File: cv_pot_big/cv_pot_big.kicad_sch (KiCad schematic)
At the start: 13 parts, among them J1 I/O connector, U1 HT7550-1, U2 TLV6001UIDBVR

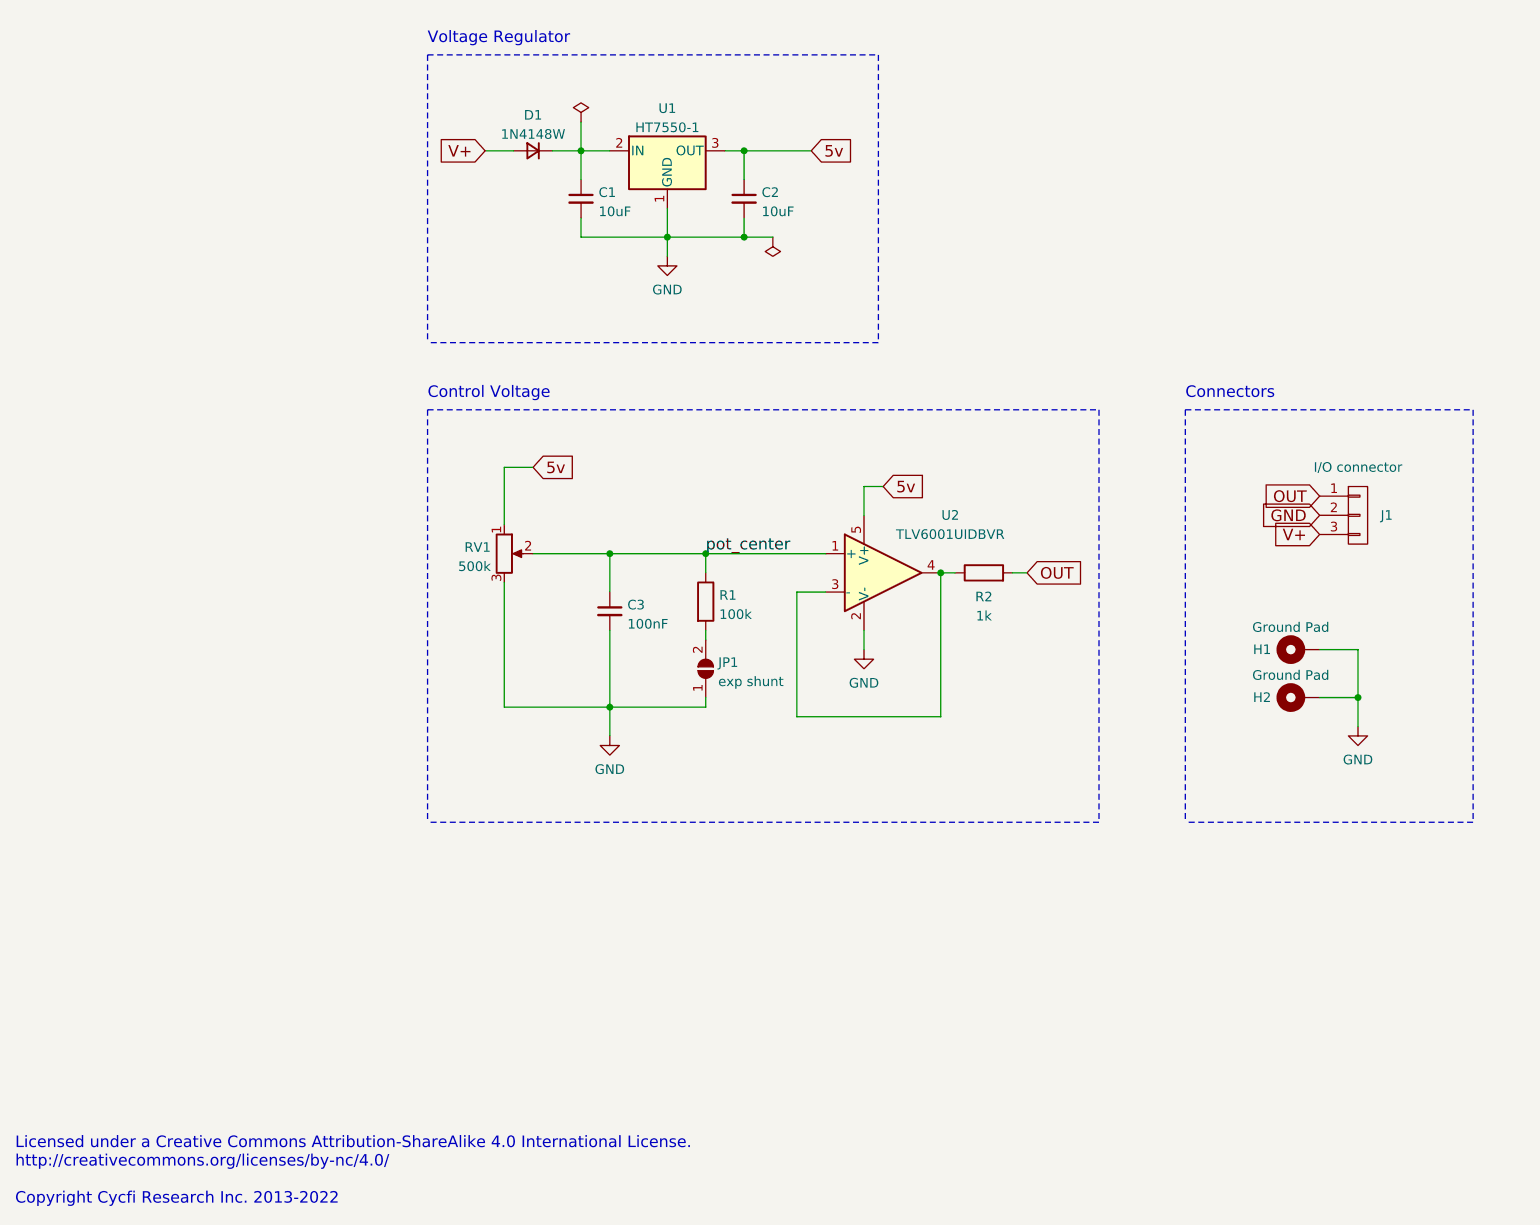
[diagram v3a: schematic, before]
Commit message: Update with log and exp taper
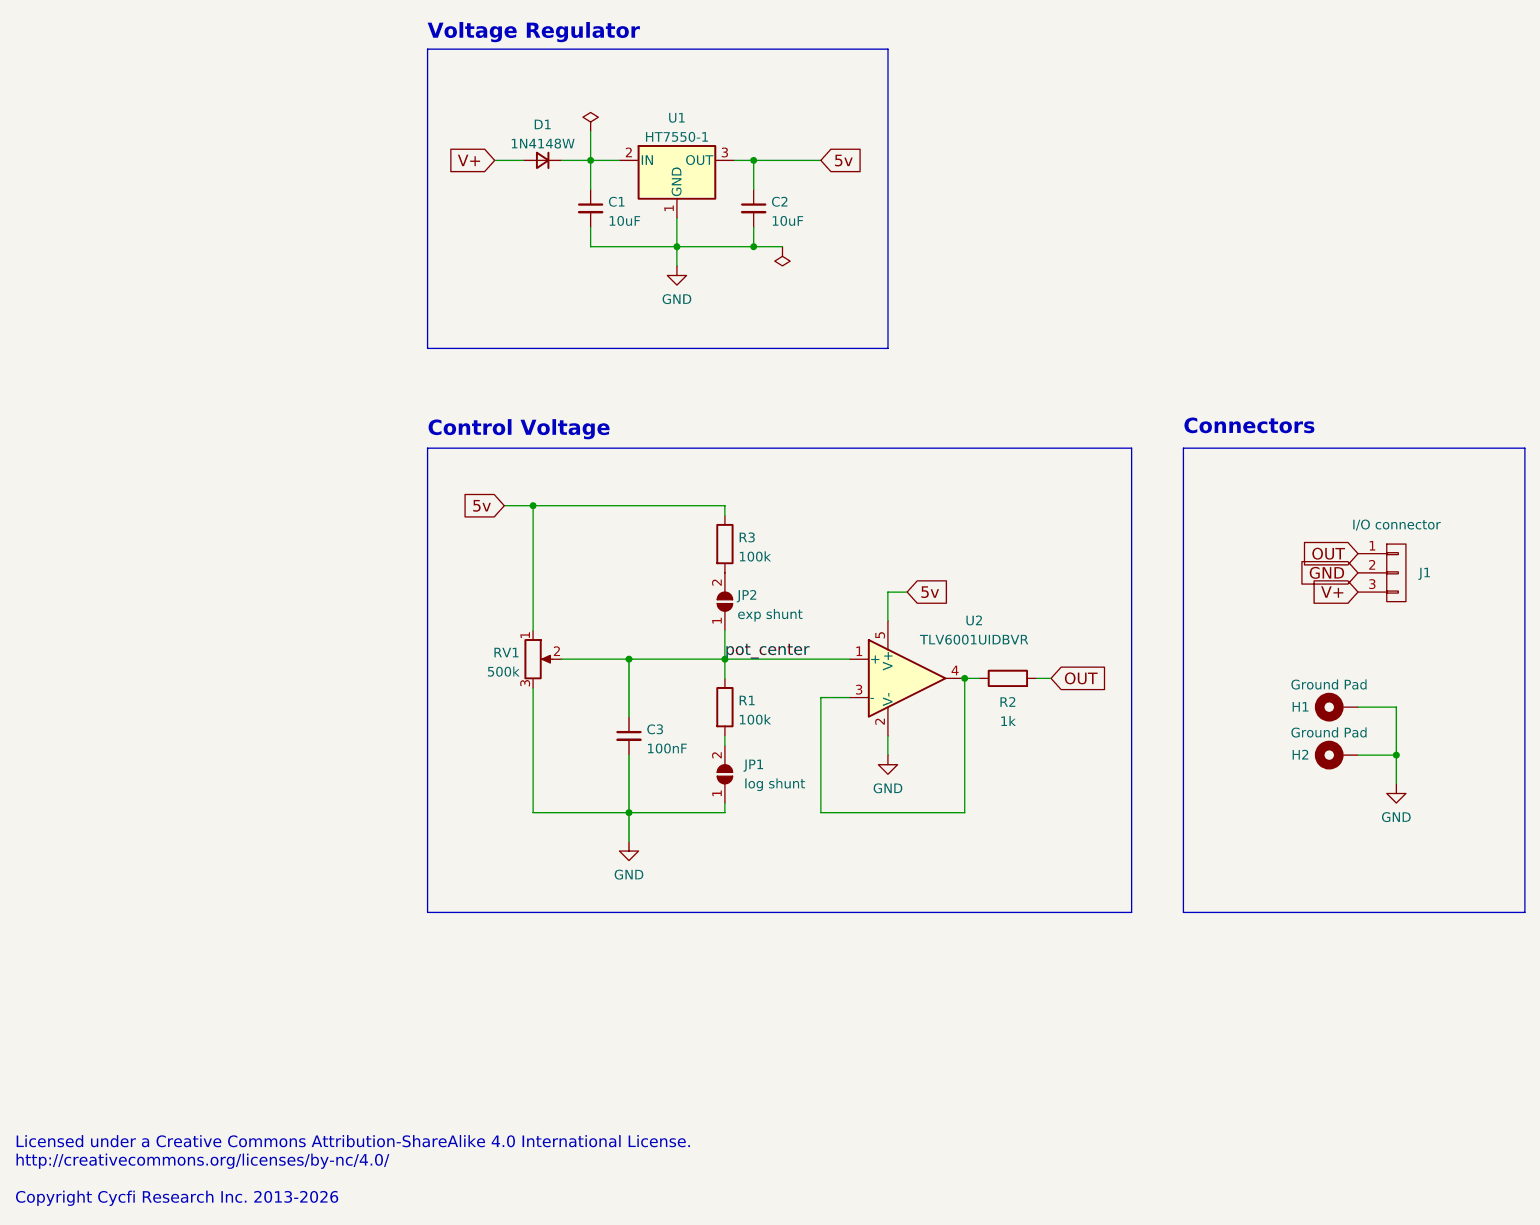
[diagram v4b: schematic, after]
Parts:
- added JP2: exp shunt, Jumper:SolderJumper-2_P1.3mm_Open_TrianglePad1.0x1.5mm, symbol Jumper:SolderJumper_2_Open
- added R3: 100k, Resistor_SMD:R_0402_1005Metric, symbol Device:R
- JP1: value exp shunt -> log shunt
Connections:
- net 5v: now also R3.1
- net pot_center: now also JP2.1 (A)
- new net: JP2.2 (B), R3.2
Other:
- note added: "Licensed under a Creative Commons Attribution-ShareAlike 4.0 International License. http://creativecommons.org/licenses/by-nc/4.0/ Copyright Cycfi Research Inc. 2013-2026"
- note removed: "Licensed under a Creative Commons Attribution-ShareAlike 4.0 International License. http://creativecommons.org/licenses/by-nc/4.0/ Copyright Cycfi Research Inc. 2013-2022"
- moved on the sheet: C1, C2, C3, D1, H1, H2, J1, JP1, R1, R2, RV1, U1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

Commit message: Change symbol to generic one
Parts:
- J1: symbol cycfi_library:conn_1x3 -> Connector_Generic:Conn_01x03
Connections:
- net pot_center renamed pot_wiper
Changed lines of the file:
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@@
 		)
 	)
-	(label "pot_center"
+	(label "pot_wiper"
 		(at 118.11 115.57 0)
 		(effects
@@
 	)
 	(symbol
-		(lib_id "cycfi_library:conn_1x3")
+		(lib_id "Connector_Generic:Conn_01x03")
 		(at 207.01 104.14 0)
 		(unit 1)
@@
 			)
 		)
-		(property "Datasheet" ""
+		(property "Datasheet" "~"
 			(at 207.01 104.14 0)
 			(effects
@@
 			)
 		)
-		(property "Description" ""
+		(property "Description" "Generic connector, single row, 01x03, script generated (kicad-library-utils/schlib/autogen/connector/)"
 			(at 207.01 104.14 0)
 			(effects
@@
 					(size 1.27 1.27)
 				)
-			)
-		)
+				(hide yes)
+			)
+		)

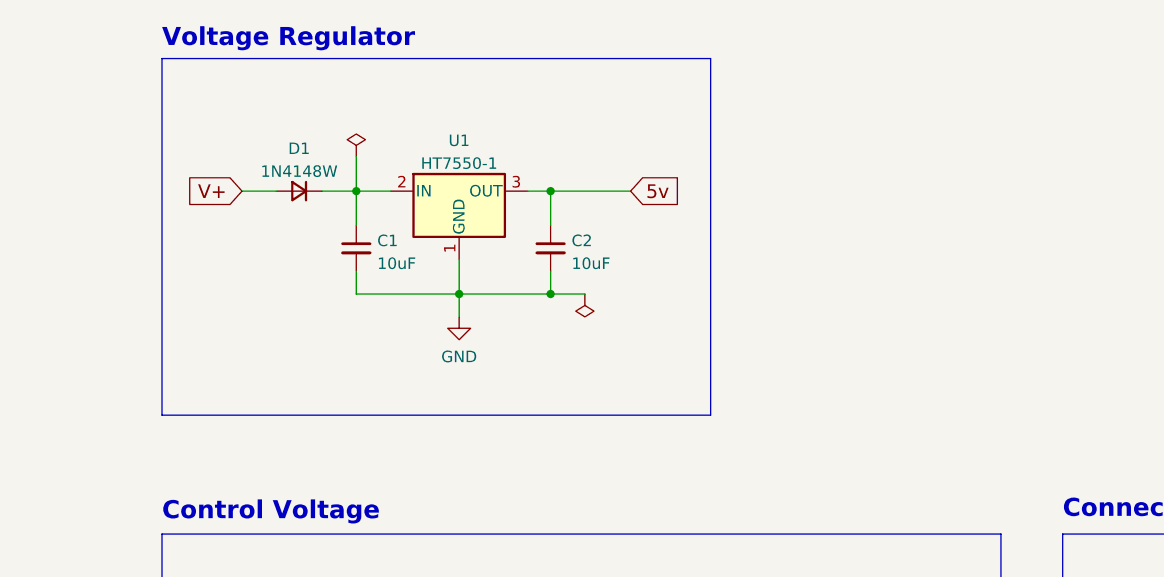
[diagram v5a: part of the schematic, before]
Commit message: Added Opamp bypass cap
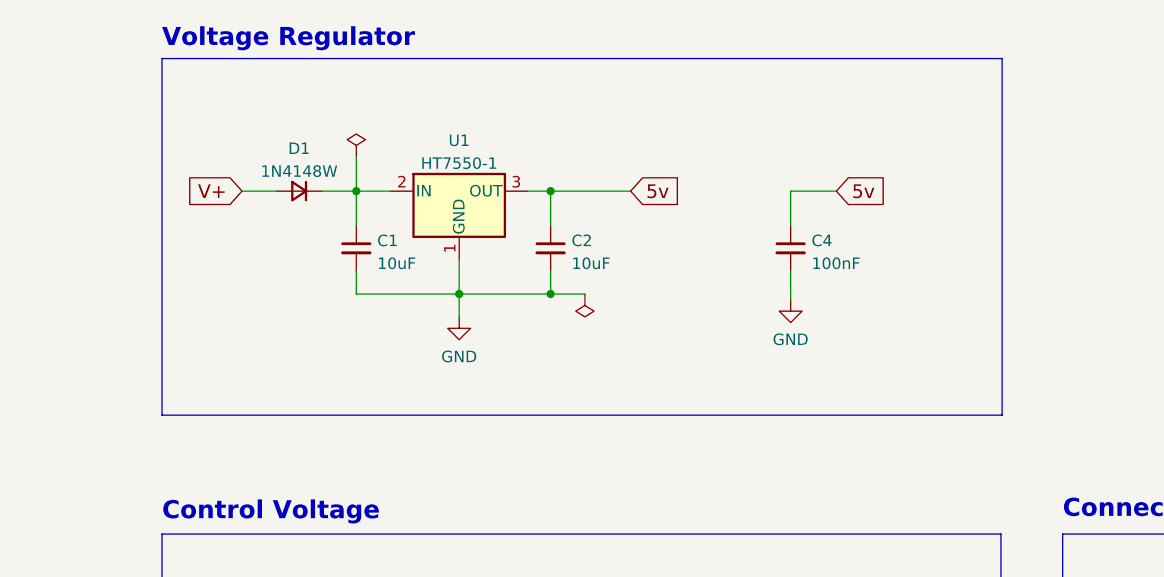
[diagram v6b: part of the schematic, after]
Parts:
- added C4: 100nF, Capacitor_SMD:C_0402_1005Metric, symbol Device:C_Small
- U2: LCSC (none) -> C544299
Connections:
- net 5v: now also C4.1
- net GND: now also C4.2
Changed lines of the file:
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@@
 	(rectangle
 		(start 78.74 34.798)
-		(end 139.7 74.422)
+		(end 172.085 74.422)
 		(stroke
 			(width 0)
@@
 	(wire
 		(pts
+			(xy 148.59 49.53) (xy 148.59 53.34)
+		)
+		(stroke
+			(width 0)
+			(type default)
+		)
+	)
+	(wire
+		(pts
 			(xy 88.9 95.25) (xy 92.71 95.25)
 		)
@@
 	(wire
 		(pts
+			(xy 153.67 49.53) (xy 148.59 49.53)
+		)
+		(stroke
+			(width 0)
+			(type default)
+		)
+	)
+	(wire
+		(pts
 			(xy 119.38 49.53) (xy 121.92 49.53)
 		)
@@
 		(pts
 			(xy 139.7 110.49) (xy 139.7 106.68)
+		)
+		(stroke
+			(width 0)
+			(type default)
+		)
+	)
+	(wire
+		(pts
+			(xy 148.59 58.42) (xy 148.59 61.595)
 		)
 		(stroke
@@
 		)
 	)
+	(global_label "5v"
+		(shape input)
+		(at 153.67 49.53 0)
+		(fields_autoplaced yes)
+		(effects
+			(font
+				(size 1.524 1.524)
+			)
+			(justify left)
+		)
+		(property "Intersheetrefs" "${INTERSHEET_REFS}"
+			(at 159.0715 49.4348 0)
+			(effects
+				(font
+					(size 1.524 1.524)
+				)
+				(justify left)
+				(hide yes)
+			)
+		)
+	)
 	(global_label "GND"
 		(shape input)
@@
 	)
 	(symbol
+		(lib_id "power:GND")
+		(at 148.59 61.595 0)
+		(unit 1)
+		(exclude_from_sim no)
+		(in_bom yes)
+		(on_board yes)
+		(dnp no)
+		(fields_autoplaced yes)
+		(property "Reference" "#PWR04"
+			(at 148.59 67.945 0)
+			(effects
+				(font
+					(size 1.27 1.27)
+				)
+				(hide yes)
+			)
+		)
+		(property "Value" "GND"
+			(at 148.59 66.0384 0)
+			(effects
+				(font
+					(size 1.27 1.27)
+				)
+			)
+		)
+		(property "Footprint" ""
+			(at 148.59 61.595 0)
+			(effects
+				(font
+					(size 1.27 1.27)
+				)
+				(hide yes)
+			)
+		)
+		(property "Datasheet" ""
+			(at 148.59 61.595 0)
+			(effects
+				(font
+					(size 1.27 1.27)
+				)
+				(hide yes)
+			)
+		)
+		(property "Description" ""
+			(at 148.59 61.595 0)
+			(effects
+				(font
+					(size 1.27 1.27)
+				)
+			)
+		)
+		(pin "1"
+		)
+		(instances
+			(project "cv_pot_big"
+				(path "/e63e39d7-6ac0-4ffd-8aa3-1841a4541b55"
+					(reference "#PWR04")
+					(unit 1)
+				)
+			)
+		)
+	)
+	(symbol
 		(lib_id "power:PWR_FLAG")
 		(at 125.73 60.96 180)
@@
 	)
 	(symbol
+		(lib_id "Device:C_Small")
+		(at 148.59 55.88 0)
+		(unit 1)
+		(exclude_from_sim no)
+		(in_bom yes)
+		(on_board yes)
+		(dnp no)
+		(fields_autoplaced yes)
+		(property "Reference" "C4"
+			(at 150.9141 55.0516 0)
+			(effects
+				(font
+					(size 1.27 1.27)
+				)
+				(justify left)
+			)
+		)
+		(property "Value" "100nF"
+			(at 150.9141 57.5885 0)
+			(effects
+				(font
+					(size 1.27 1.27)
+				)
+				(justify left)
+			)
+		)
+		(property "Footprint" "Capacitor_SMD:C_0402_1005Metric"
+			(at 148.59 55.88 0)
+			(effects
+				(font
+					(size 1.27 1.27)
+				)
+				(hide yes)
+			)
+		)
+		(property "Datasheet" "~"
+			(at 148.59 55.88 0)
+			(effects
+				(font
+					(size 1.27 1.27)
+				)
+				(hide yes)
+			)
+		)
+		(property "Description" ""
+			(at 148.59 55.88 0)
+			(effects
+				(font
+					(size 1.27 1.27)
+				)
+			)
+		)
+		(property "LCSC" "C307331"
+			(at 148.59 55.88 0)
+			(effects
+				(font
+					(size 1.524 1.524)
+				)
+				(hide yes)
+			)
+		)
+		(pin "1"
+		)
+		(pin "2"
+		)
+		(instances
+			(project "cv_pot_big"
+				(path "/e63e39d7-6ac0-4ffd-8aa3-1841a4541b55"
+					(reference "C4")
+					(unit 1)
+				)
+			)
+		)
+	)
+	(symbol
 		(lib_id "Device:R")
 		(at 118.11 100.33 0)
@@
 			)
 		)
+		(property "LCSC" "C544299"
+			(at 142.24 118.11 0)
+			(effects
+				(font
+					(size 1.27 1.27)
+				)
+				(hide yes)
+			)
+		)

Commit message: - CV pot big updates for Fab - Added SMD 1x3P header
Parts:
- H1, H2, RV1: now left out of the parts list
- J1: JLCPCB_CORRECTION (none) -> 0;0;90; LCSC (none) -> C5242196
- U1, U2: JLCPCB_CORRECTION (none) -> 0;0;180
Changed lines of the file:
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@@
 		(unit 1)
 		(exclude_from_sim no)
-		(in_bom yes)
+		(in_bom no)
 		(on_board yes)
 		(dnp no)
@@
 			)
 		)
+		(property "JLCPCB_CORRECTION" "0;0;180"
+			(at 111.76 49.53 0)
+			(effects
+				(font
+					(size 1.524 1.524)
+				)
+				(hide yes)
+			)
+		)
 		(pin "1"
 		)
@@
 		(unit 1)
 		(exclude_from_sim no)
-		(in_bom yes)
+		(in_bom no)
 		(on_board yes)
 		(dnp no)
@@
 		(unit 1)
 		(exclude_from_sim no)
-		(in_bom yes)
+		(in_bom no)
 		(on_board yes)
 		(dnp no)
@@
 			)
 		)
+		(property "LCSC" "C5242196"
+			(at 207.01 104.14 0)
+			(effects
+				(font
+					(size 1.524 1.524)
+				)
+				(hide yes)
+			)
+		)
+		(property "JLCPCB_CORRECTION" "0;0;90"
+			(at 207.01 104.14 0)
+			(effects
+				(font
+					(size 1.524 1.524)
+				)
+				(hide yes)
+			)
+		)
 		(pin "1"
 		)
@@
 				)
 				(hide yes)
+			)
+		)
+		(property "JLCPCB_CORRECTION" "0;0;180"
+			(at 142.24 118.11 0)
+			(effects
+				(font
+					(size 1.524 1.524)
+				)
+				(hide yes)
